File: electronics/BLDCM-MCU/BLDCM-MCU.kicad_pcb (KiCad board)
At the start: 4 copper layers, 32 x 32 mm, 89 parts, among them J1 52991-0308, K1 EVPAKE31A, U1 STM32F446RE, U10 SK6805, U11 SK6805, U12 SK6805, U13 SK6805, U14 SK6805, U15 SK6805, U16 SK6805, U17 SK6805, U18 SK6805, U19 SK6805, U2 SN74LV1T34DBVR, U20 MT6701, U3 ISM330DHCX, U4 SK6805, U5 SK6805, U6 SK6805, U7 SK6805, U8 SK6805, U9 SK6805, Y1 ECS-3225MVLC-240-CN

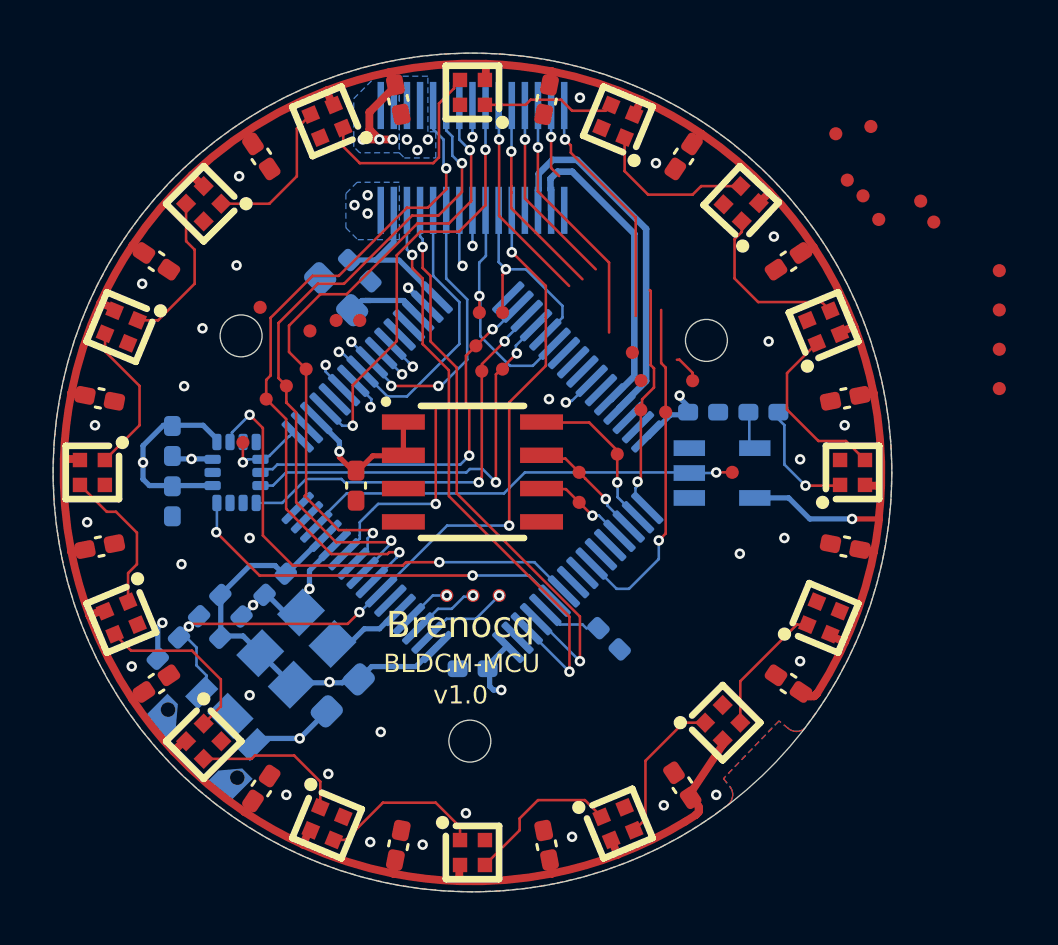
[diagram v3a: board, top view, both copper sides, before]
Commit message: Feat(pcb): Initial MCU PCB routing
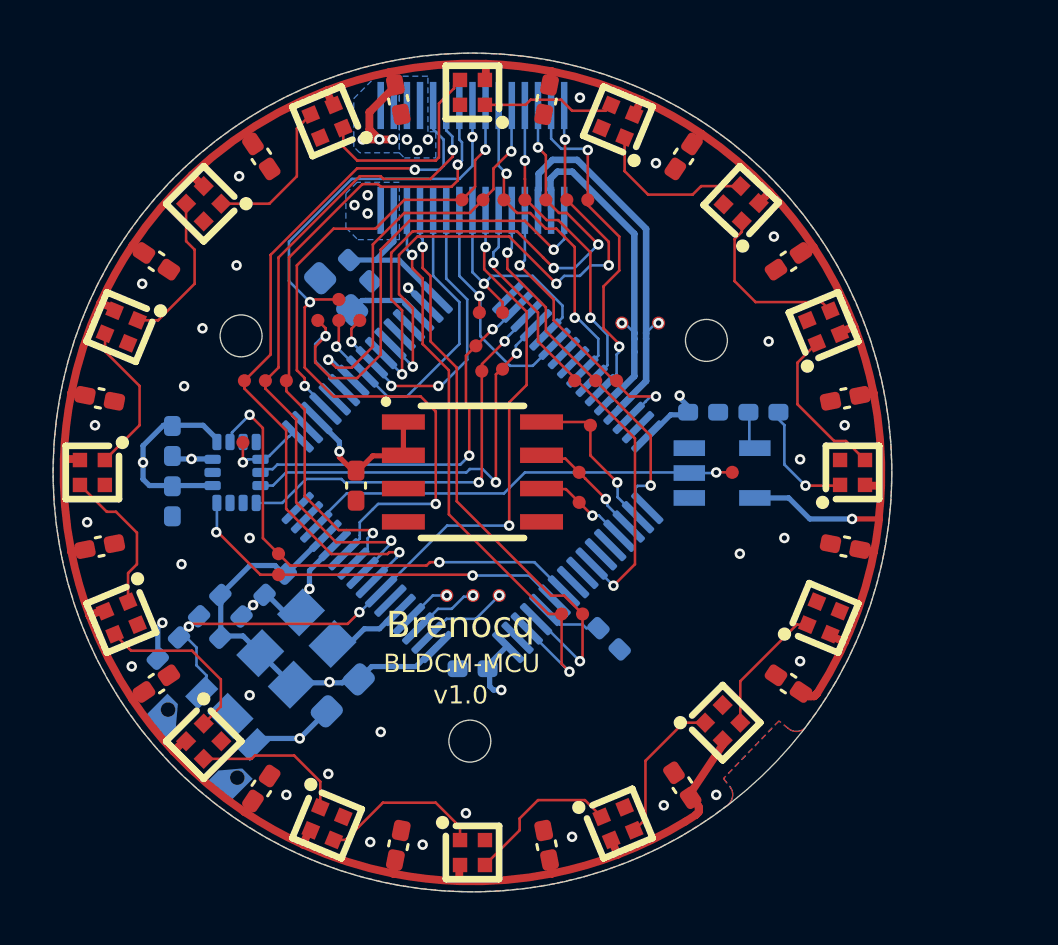
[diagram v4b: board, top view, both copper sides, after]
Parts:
- moved TP35 28.6 mm to (141.1, 108.1)
- moved TP36 28.4 mm to (141.1, 108.9)
- moved TP16 21.6 mm to (152.7, 110.4)
- moved TP18 21.1 mm to (151.9, 110.4)
- moved TP25 20.7 mm to (148.1, 94.6)
- moved TP15 17.2 mm to (148.9, 94.6)
- moved TP34 16.2 mm to (153.0, 103.2)
- moved TP17 14.3 mm to (149.7, 94.6)
- moved TP4 13.5 mm to (152.1, 94.6)
- moved TP19 12.3 mm to (150.5, 94.6)
- moved TP2 12.1 mm to (151.3, 94.6)
- moved TP21 6.07 mm to (152.9, 94.6)
- moved TP8 3.67 mm to (152.4, 101.5)
- moved TP9 3.01 mm to (143.4, 98.4)
- moved TP32 2.92 mm to (153.2, 101.5)
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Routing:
- net /VOLT.U: track 9.46 -> 30.7 mm, vias 2 -> 3
- net /VOLT.SRC: track 1.25 -> 20.9 mm, vias 1 -> 2
- net /TMC.WL: track 10.4 -> 21.9 mm, vias 2 -> 4
- net /SWDIO: track 0.00 -> 11.3 mm, vias 0 -> 2
- net /TMC.VL: track 10.9 -> 21.6 mm, vias 2 -> 4
- net /TMC.WH: track 2.82 -> 13.3 mm, vias 1 -> 2
- net /TMC.UL: track 9.07 -> 16.3 mm, vias 3 -> 2
- net /SWCLK: track 8.87 -> 14.4 mm, vias 1 -> 2
- net /SWO: track 13.1 -> 18.2 mm, vias 1 -> 2
- net /TMC.UH: track 7.98 -> 12.6 mm, vias 1 -> 2
- net /TMC.VH: track 8.69 -> 12.3 mm
- net /VCP.RX: track 11.5 -> 9.54 mm, vias 2 -> 1
- net /CURR.U: track 26.5 -> 27.9 mm
- net /VOLT.V: track 11.6 -> 12.9 mm
- net /VOLT.W: track 11.7 -> 12.6 mm
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
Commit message: Fix(pcb): MCU PCB DRC errors
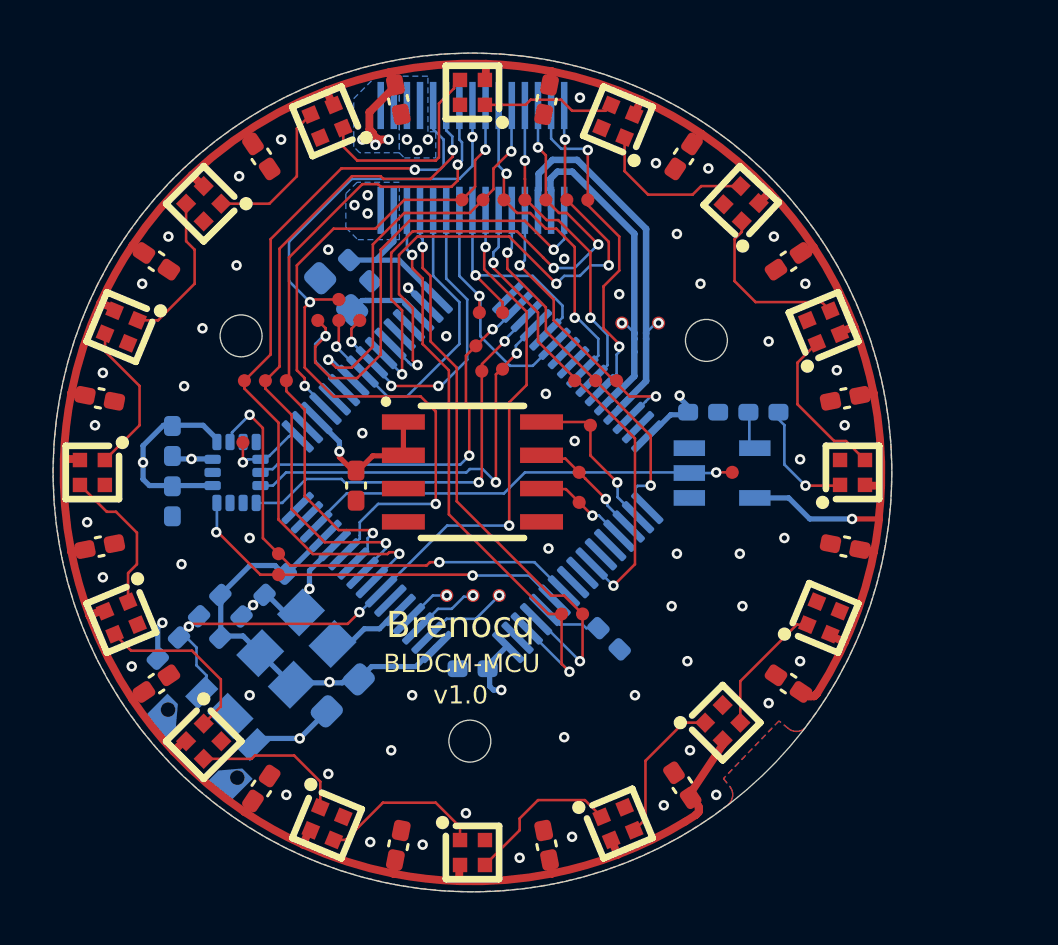
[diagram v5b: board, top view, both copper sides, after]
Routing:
- net /CURR.U: track 27.9 -> 28.7 mm
- net GND: vias 38 -> 65

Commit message: Feat: v1.0 MCU/Power PCBs ready
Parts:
- added C28: 10uF, BrenoCQ:C_0805, F.Cu at (154.2, 105.9)
- added TP37: Test point 0.5mm, BrenoCQ:TP_0.5mm, F.Cu at (155.2, 109.4)
- C1: footprint BrenoCQ:C_0603 -> BrenoCQ:C_0402
- U20: value MT6701 -> AS5048A; footprint BrenoCQ:SOP-8 -> BrenoCQ:TSSOP-14
- moved C27 9.60 mm to (153.6, 104.4), turned to 180 degrees
- moved TP34 6.17 mm to (157.0, 107.9)
- moved TP20 5.13 mm to (156.4, 108.4)
- moved TP22 4.25 mm to (155.8, 108.9)
- moved TP36 1.61 mm to (139.7, 108.1)
- moved TP35 0.60 mm to (140.5, 108.1)
- moved K1 0.07 mm to (138.4, 115.2)
- turned U2 to 90 degrees
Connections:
- U1 pad 53: unconnected-(U1C-PC12-Pad53) -> /ENC.PICO
- U20 pad 1: 3.3V -> /ENC.CS
- U20 pad 2: 3.3V -> /ENC.CLK
- U20 pad 3: unconnected-(U20-OUT-Pad3) -> /ENC.POCI
- U20 pad 4: GND -> /ENC.PICO
- U20 pad 6: /ENC.POCI -> unconnected-(U20-TEST-Pad6)
- U20 pad 7: /ENC.CLK -> unconnected-(U20-TEST-Pad7)
- U20 pad 8: /ENC.CS -> unconnected-(U20-TEST-Pad8)
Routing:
- net /ENC.PICO: track 0.00 -> 13.7 mm, vias 0 -> 1
- net /ENC.POCI: track 3.71 -> 14.7 mm
- net /ENC.CLK: track 4.55 -> 15.3 mm
- net /ENC.CS: track 6.19 -> 16.4 mm
- net /CAN.TX: track 22.8 -> 29.9 mm
- net /CAN.RX: track 22.4 -> 29.6 mm
- net /VOLT.U: track 30.7 -> 25.2 mm
- net /SWO: track 18.2 -> 23.3 mm
- net /CURR.W: track 24.8 -> 28.1 mm
- net /SWCLK: track 14.4 -> 17.0 mm
- net /IMU.INT2: track 18.7 -> 20.9 mm
- net /IMU.CLK: track 14.8 -> 16.1 mm
- net /IMU.INT1: track 15.1 -> 16.2 mm
- net /IMU.POCI: track 16.0 -> 16.9 mm
- net 3.3V: track 41.3 -> 41.7 mm, vias 8 -> 9
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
